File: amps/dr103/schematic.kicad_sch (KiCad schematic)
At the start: 97 parts, among them T1 OT

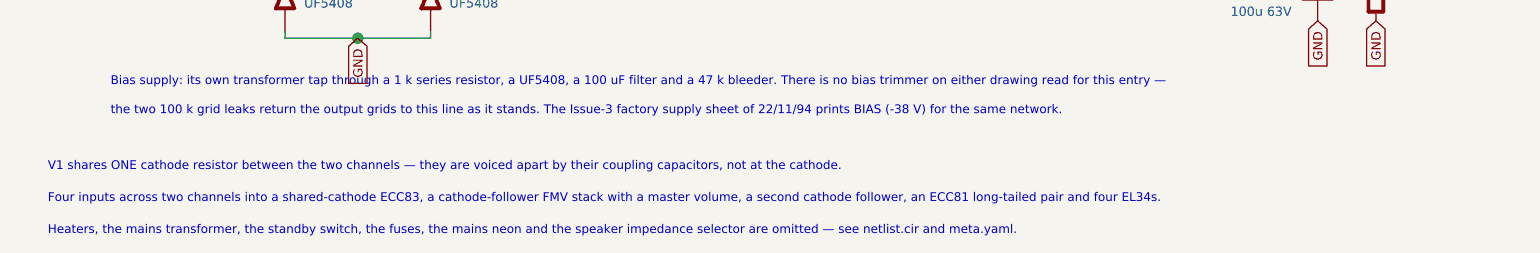
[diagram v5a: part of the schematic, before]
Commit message: Fix: schematic sheet notes no longer name repository files
Thirty-seven committed sheets rendered footnotes and section notes such as
"Heaters and PT primary omitted — see netlist.cir and meta.yaml" or
"excluded from netlist.cir (notes.md)" to visitors through KiCanvas. The
prose sweeps never counted sheets. Rewritten in the site's own words — the
netlist, the sources list, the circuit story, the parts list, the board
drawing — in 59 strings across 33 draw scripts, keeping every technical
claim as it was; the three tone sheets (6G4, 6G5, 6G6-B) are under repair
elsewhere and keep theirs for now. The sweep touched only strings passed to
the sheet's note, text, caption and footnote calls, never a path or a value.

Gates: check_schematics 40/0, connectivity 0 isolated pins;
verify_schematic_nets 40 clean; only the regenerated sheets and their served
copies changed.

Co-Authored-By: Claude Fable 5.1 <noreply@anthropic.com>
Claude-Session: https://claude.ai/code/session_01KBMfdh37HmCL2iWcBiL5J1
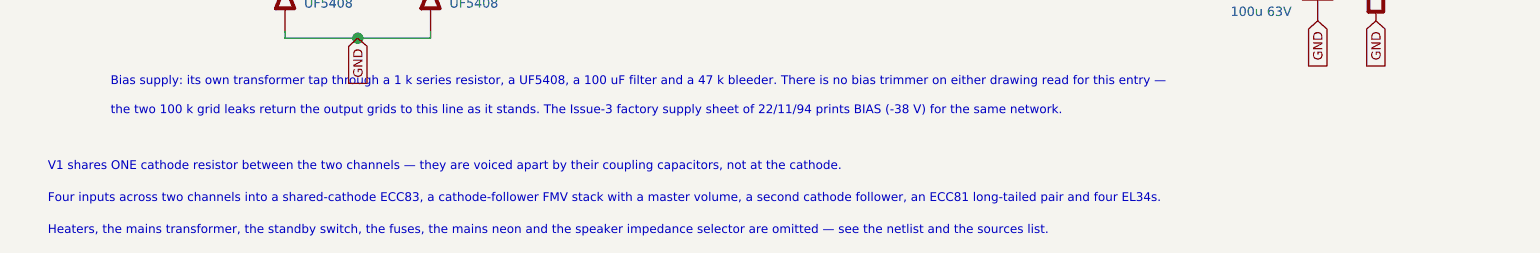
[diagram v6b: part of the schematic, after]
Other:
- note added: "Heaters, the mains transformer, the standby switch, the fuses, the mains neon and the speaker impedance selector are omitted — see the netlist and the sources list."
- note removed: "Heaters, the mains transformer, the standby switch, the fuses, the mains neon and the speaker impedance selector are omitted — see netlist.cir and meta.yaml."
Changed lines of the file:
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@@
   (text "Four inputs across two channels into a shared-cathode ECC83, a cathode-follower FMV stack with a master volume, a second cathode follower, an ECC81 long-tailed pair and four EL34s." (at 12.7 280.358 0)
     (effects (font (size 1.2 1.2)) (justify left)))
-  (text "Heaters, the mains transformer, the standby switch, the fuses, the mains neon and the speaker impedance selector are omitted — see netlist.cir and meta.yaml." (at 12.7 284.758 0)
+  (text "Heaters, the mains transformer, the standby switch, the fuses, the mains neon and the speaker impedance selector are omitted — see the netlist and the sources list." (at 12.7 284.758 0)
     (effects (font (size 1.2 1.2)) (justify left)))
   (sheet_instances (path "/" (page "1")))

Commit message: Fix: state the datasheet unit on 17 dual-triode sections whose sheets printed the other half's pin numbers
The sheet-vs-board gate reported these sockets as SECTION-SWAP; the
2026-09-10 source-read triage found the BOARD right on every one of them
(and both surfaces wrong on the 5G9 tremolo bottle). Each sheet had
lettered the section on the default map (A -> unit 1 -> pins 6/7/8) where
the factory drawing puts that stage on 1/2/3. The draw scripts now state
`unit=` on both halves, with the source cited beside the call, so the
printed socket numbers are the factory's:

- 5f4 V3: driver V3A -> 1/2/3, cathodyne V3B -> 6/7/8
  (crop 5f4-V3-layout-trace.png: +213 V driver plate -> pin 1, +270 V -> 6)
- 5f8a V3: 82k half V3A -> 1/2/3, 100k half V3B -> 6/7/8
  (crop 5f8a-V3-layout-trace.png: +225 -> 6, +19 -> 2, +28.5 -> 8)
- 6161 V1: channel 1 V1A -> 1/2/3 (crop 6161-V1-ch1.png prints 1/2/3);
  6161 V2: 1 MEG-grid half V2A -> 1/2/3, paraphase V2B -> 6/7/8
  (crop 6161-V2.png / 6161-V2-right.png)
- 6g3 V3: 82k half V3A -> 1/2/3 (crop 6g3-V3-layout-wires.png: +230 -> 1,
  +225 -> 6, +20 -> 7)
- aa1164 V3: recovery V3A -> 1/2/3, mixer V3B -> 6/7/8
  (crops aa1164-V3A-recovery-schem.png, aa1164-V3B-mixer-schem.png)
- aa864-bassman V1/V2: input stages 2/1/3, second stages 7/6/8; V4: the
  .1/500 pF-fed 82k half 2/1/3 (crops aa864-V1A-input.png,
  aa864-V1B-second.png, aa864-V2A-input.png, aa864-V2B-second.png,
  aa864-V4-PI.png)
- ab165 V1/V2/V4: same pattern (crops ab165-V1A-input.png,
  ab165-V1B-second.png, ab165-V2A-input.png, ab165-V2B-second.png,
  ab165-V4-PI.png)
- ab763-super V1/V2: slope-plate +270 V -> pin 1 (input stage), .047
  plate -> 6 (crops ab763-super-V1-layout-sh.png, ab763-super-V2-layout-sh.png)
- dr103 V2/V3: gain stages 6/7/8, cathode followers 1/2/3 (crops
  dr103-V2-huss.png, dr103-V3-huss.png — the Huss redraw, not a factory
  print; noted in the script)
- 5g9 V3: oscillator V3A -> 1/2/3, follower V3B -> 6/7/8 (crops
  5g9-V3-strap71-zoom.png, 5g9-V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
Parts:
- V2A, V3A: Basing_unit (none) -> 2
- V2B, V3B: Basing_unit (none) -> 1
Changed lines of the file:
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@@
     (in_bom yes) (on_board yes)
     (property "Reference" "V2B" (at 109.249 126.558 0) (effects (font (size 1.27 1.27)) (justify left)))
-    (property "Value" "ECC83" (at 109.249 128.958 0) (effects (font (size 1.27 1.27)) (justify left))))
+    (property "Value" "ECC83" (at 109.249 128.958 0) (effects (font (size 1.27 1.27)) (justify left)))
+    (property "Basing_unit" "1" (at 109.249 131.358 0) (effects (font (size 1.27 1.27)) hide)))
   (wire (pts (xy 111.336 126.278) (xy 113.716 126.278))
     (stroke (width 0) (type default)))
@@
     (in_bom yes) (on_board yes)
     (property "Reference" "V2A" (at 143.336 119.878 0) (effects (font (size 1.27 1.27)) (justify left)))
-    (property "Value" "ECC83 CF" (at 143.336 122.278 0) (effects (font (size 1.27 1.27)) (justify left))))
+    (property "Value" "ECC83 CF" (at 143.336 122.278 0) (effects (font (size 1.27 1.27)) (justify left)))
+    (property "Basing_unit" "2" (at 143.336 124.678 0) (effects (font (size 1.27 1.27)) hide)))
   (wire (pts (xy 129.336 115.178) (xy 129.336 126.278))
     (stroke (width 0) (type default)))
@@
     (in_bom yes) (on_board yes)
     (property "Reference" "V3B" (at 217.336 119.878 0) (effects (font (size 1.27 1.27)) (justify left)))
-    (property "Value" "ECC83" (at 217.336 122.278 0) (effects (font (size 1.27 1.27)) (justify left))))
+    (property "Value" "ECC83" (at 217.336 122.278 0) (effects (font (size 1.27 1.27)) (justify left)))
+    (property "Basing_unit" "1" (at 217.336 124.678 0) (effects (font (size 1.27 1.27)) hide)))
   (wire (pts (xy 196.416 110.088) (xy 200.336 110.088))
     (stroke (width 0) (type default)))
@@
     (in_bom yes) (on_board yes)
     (property "Reference" "V3A" (at 247.336 119.878 0) (effects (font (size 1.27 1.27)) (justify left)))
-    (property "Value" "ECC83 CF" (at 247.336 122.278 0) (effects (font (size 1.27 1.27)) (justify left))))
+    (property "Value" "ECC83 CF" (at 247.336 122.278 0) (effects (font (size 1.27 1.27)) (justify left)))
+    (property "Basing_unit" "2" (at 247.336 124.678 0) (effects (font (size 1.27 1.27)) hide)))
   (wire (pts (xy 230.336 126.278) (xy 233.716 126.278))
     (stroke (width 0) (type default)))
@@
   (text "3" (at 56.186 86.628 0)
     (effects (font (size 1.1 1.1)) (justify left)))
-  (text "1" (at 122.186 119.928 0)
-    (effects (font (size 1.1 1.1)) (justify left)))
-  (text "2" (at 114.389 124.878 0)
-    (effects (font (size 1.1 1.1)) (justify left)))
-  (text "3" (at 122.186 132.628 0)
-    (effects (font (size 1.1 1.1)) (justify left)))
-  (text "6" (at 138.186 119.928 0)
-    (effects (font (size 1.1 1.1)) (justify left)))
-  (text "7" (at 130.389 124.878 0)
-    (effects (font (size 1.1 1.1)) (justify left)))
-  (text "8" (at 138.186 132.628 0)
-    (effects (font (size 1.1 1.1)) (justify left)))
-  (text "1" (at 212.186 119.928 0)
-    (effects (font (size 1.1 1.1)) (justify left)))
-  (text "2" (at 204.389 124.878 0)
-    (effects (font (size 1.1 1.1)) (justify left)))
-  (text "3" (at 212.186 132.628 0)
-    (effects (font (size 1.1 1.1)) (justify left)))
-  (text "6" (at 242.186 119.928 0)
-    (effects (font (size 1.1 1.1)) (justify left)))
-  (text "7" (at 234.389 124.878 0)
-    (effects (font (size 1.1 1.1)) (justify left)))
-  (text "8" (at 242.186 132.628 0)
+  (text "6" (at 122.186 119.928 0)
+    (effects (font (size 1.1 1.1)) (justify left)))
+  (text "7" (at 114.389 124.878 0)
+    (effects (font (size 1.1 1.1)) (justify left)))
+  (text "8" (at 122.186 132.628 0)
+    (effects (font (size 1.1 1.1)) (justify left)))
+  (text "1" (at 138.186 119.928 0)
+    (effects (font (size 1.1 1.1)) (justify left)))
+  (text "2" (at 130.389 124.878 0)
+    (effects (font (size 1.1 1.1)) (justify left)))
+  (text "3" (at 138.186 132.628 0)
+    (effects (font (size 1.1 1.1)) (justify left)))
+  (text "6" (at 212.186 119.928 0)
+    (effects (font (size 1.1 1.1)) (justify left)))
+  (text "7" (at 204.389 124.878 0)
+    (effects (font (size 1.1 1.1)) (justify left)))
+  (text "8" (at 212.186 132.628 0)
+    (effects (font (size 1.1 1.1)) (justify left)))
+  (text "1" (at 242.186 119.928 0)
+    (effects (font (size 1.1 1.1)) (justify left)))
+  (text "2" (at 234.389 124.878 0)
+    (effects (font (size 1.1 1.1)) (justify left)))
+  (text "3" (at 242.186 132.628 0)
     (effects (font (size 1.1 1.1)) (justify left)))
   (text "6" (at 268.186 95.928 0)
